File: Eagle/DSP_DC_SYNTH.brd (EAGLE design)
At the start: 100 x 100 mm, 83 parts, among them J16 U.FL_CONN, J17 U.FL_CONN, J2 3.5HEADPHONEJACK, J5 U.FL_CONN, J6 U.FL_CONN, U1 5V_REG, U2 MIXER, U3 DUAL_OP_AMP_LMV822, U4 DIGITAL_POTDIGITAL_POT, U5 TC1185-3.3VCT713, U6 LMX2326, U7 MAX2752, U8 RMK-3-93+

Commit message: mo laying out
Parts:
- moved C1 56.9 mm to (8.89, 78.1), turned to 180 degrees
- moved C2 54.1 mm to (17.1, 73.0), turned to 90 degrees
- moved U1 47.7 mm to (11.7, 72.4), turned to 180 degrees
- moved J3 1.59 mm to (2.86, 69.5)
- moved J1 1.59 mm to (2.86, 77.8)
- moved J4 1.59 mm to (2.86, 73.7)
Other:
- board text added: "GND +9V"
- board text removed: "+9V GND"

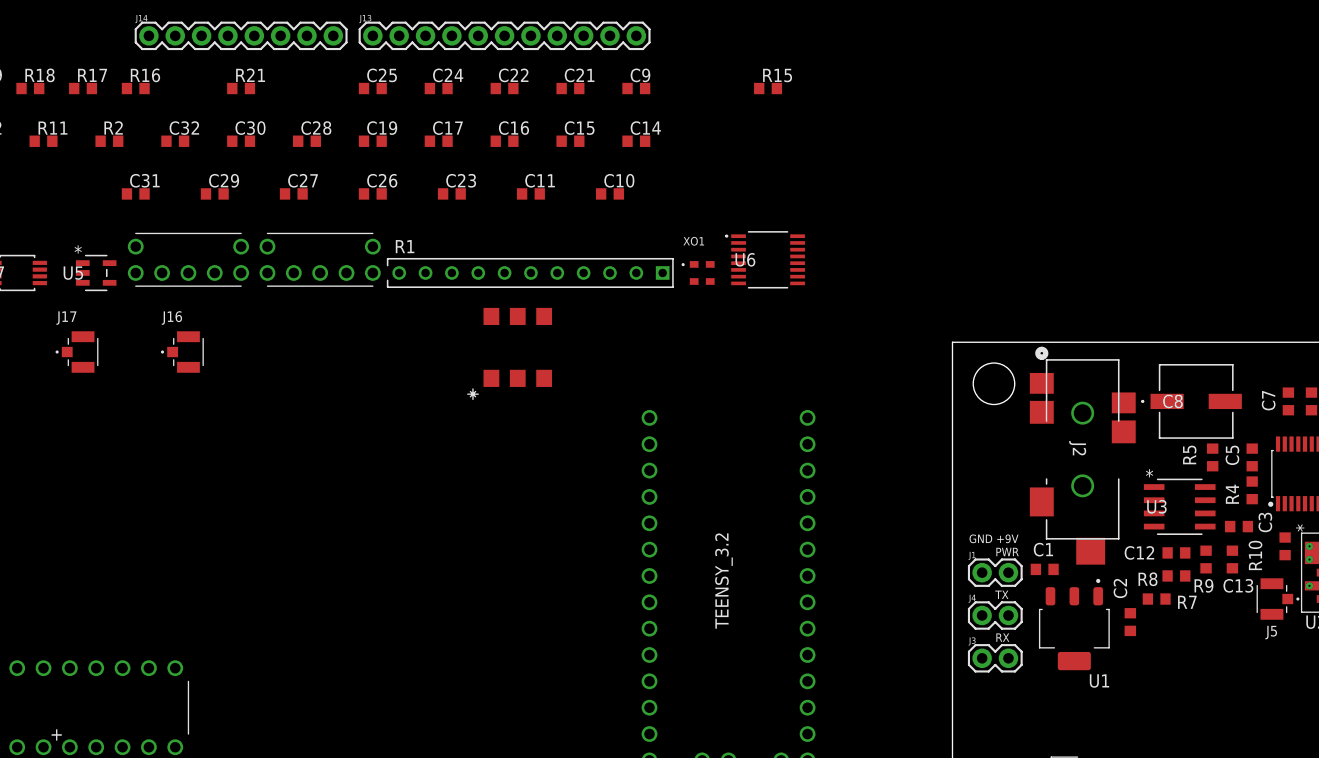
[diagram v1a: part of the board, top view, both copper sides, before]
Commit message: All the mixer stuff is placed
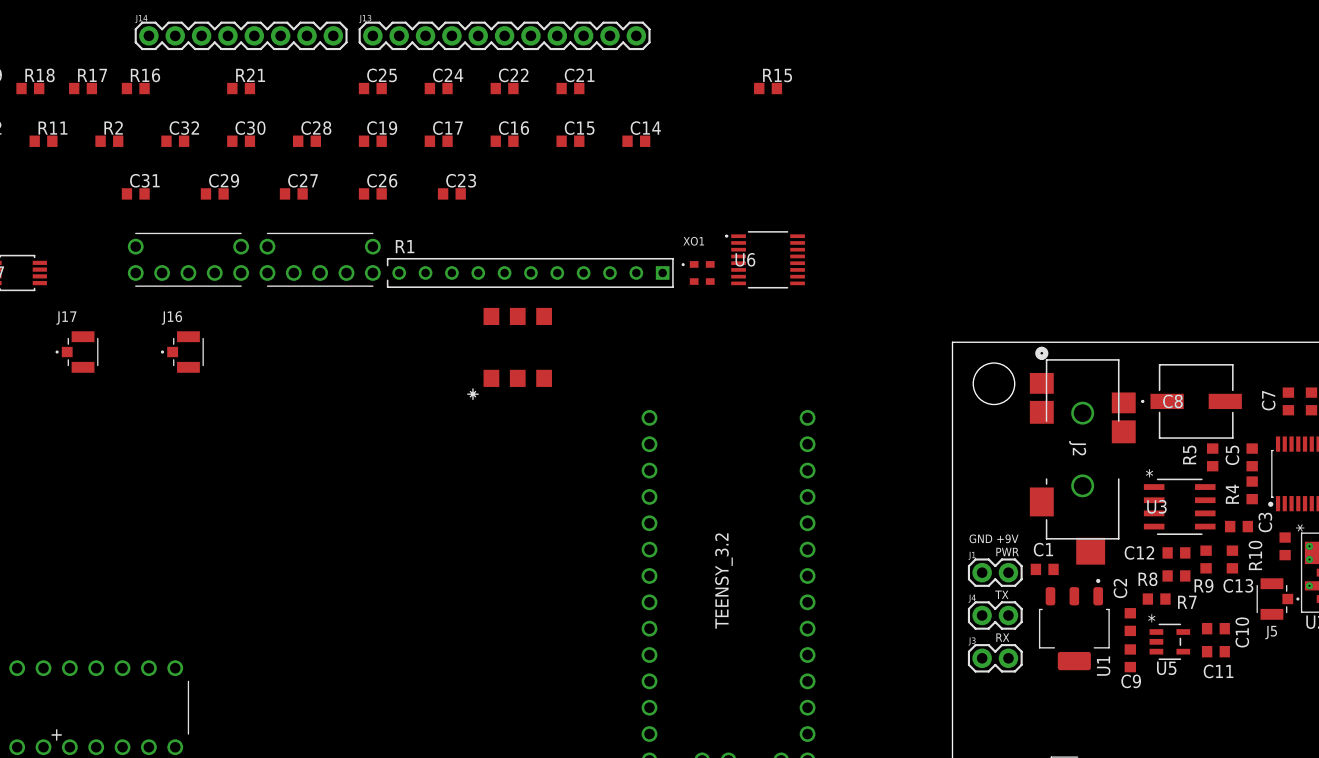
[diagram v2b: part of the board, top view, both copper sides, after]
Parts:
- moved U5 109.4 mm to (21.0, 71.1)
- moved C11 79.4 mm to (25.4, 70.2)
- moved C9 72.7 mm to (17.1, 69.5), turned to 270 degrees
- moved C10 71.9 mm to (25.4, 72.4)

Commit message: starting dsp layout
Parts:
- removed J16: U.FL_CONN, 764Library:U.FL
- added J7: (no value), SparkFun-Connectors:1X02
- moved D1 187.0 mm to (87.0, 89.5), turned to 180 degrees
- moved S2 186.0 mm to (95.9, 45.1), turned to 270 degrees
- moved TEENSY_3.2 119.5 mm to (89.5, 79.4), turned to 270 degrees
- moved R1 118.3 mm to (89.5, 92.7)
- moved S1 105.1 mm to (8.26, 34.9), turned to 90 degrees
- moved J14 64.0 mm to (-26.0, 91.4)
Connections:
- removed net N$39: J15.3, J16.1
- new net EXT_REF: J15.3, J7.1
- net GND: now also J7.2; no longer J16.2, J16.3
